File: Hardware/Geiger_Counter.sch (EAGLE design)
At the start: 54 parts, among them Q1 MPSA42, Q2 MPSA18, Q3 MMBT4403, Q4 MPSA18, U10 FT232RL-BASICSSOP, U17 AVR_SPI_PRG_6PTH, U7 TRANSFORMERAUDIO, U8 ATMEGA168, X1 USBSMD

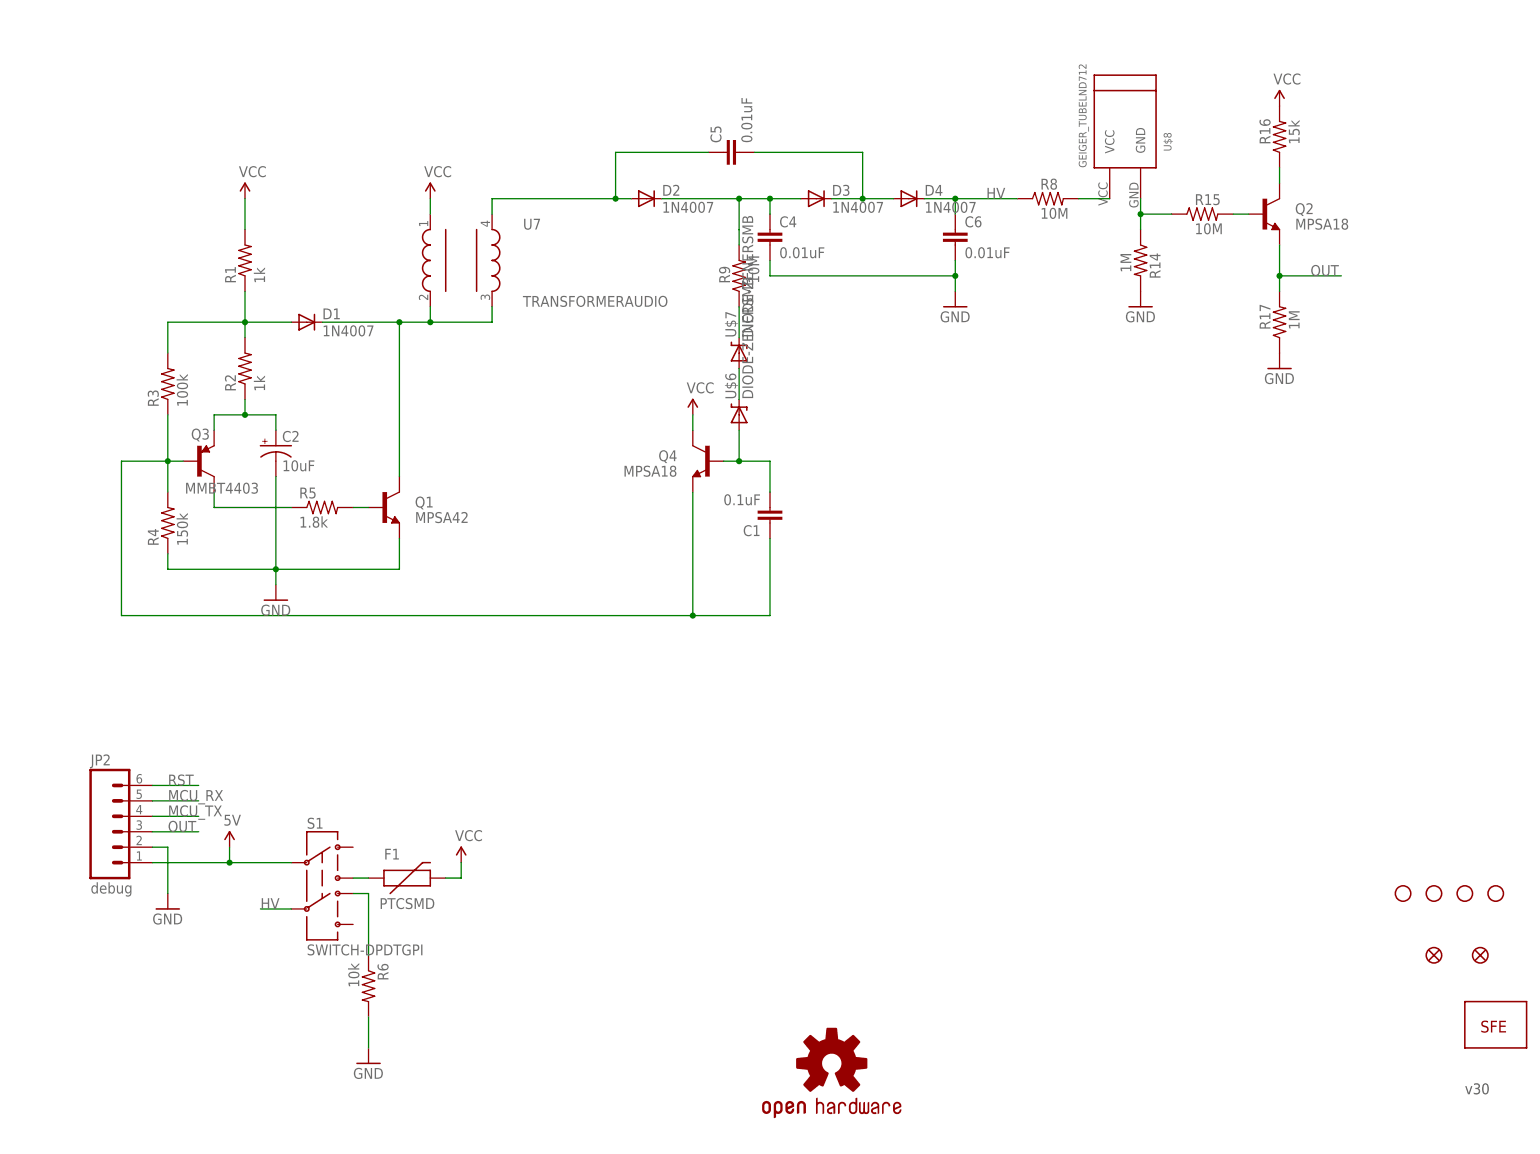
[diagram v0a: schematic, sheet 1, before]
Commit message: Updated cap/res trace re work
Updated all caps and res to 0603
Re routed y junctions to "t" junctions
Added "high voltage" to btm silk
updated schematic to frame letter.
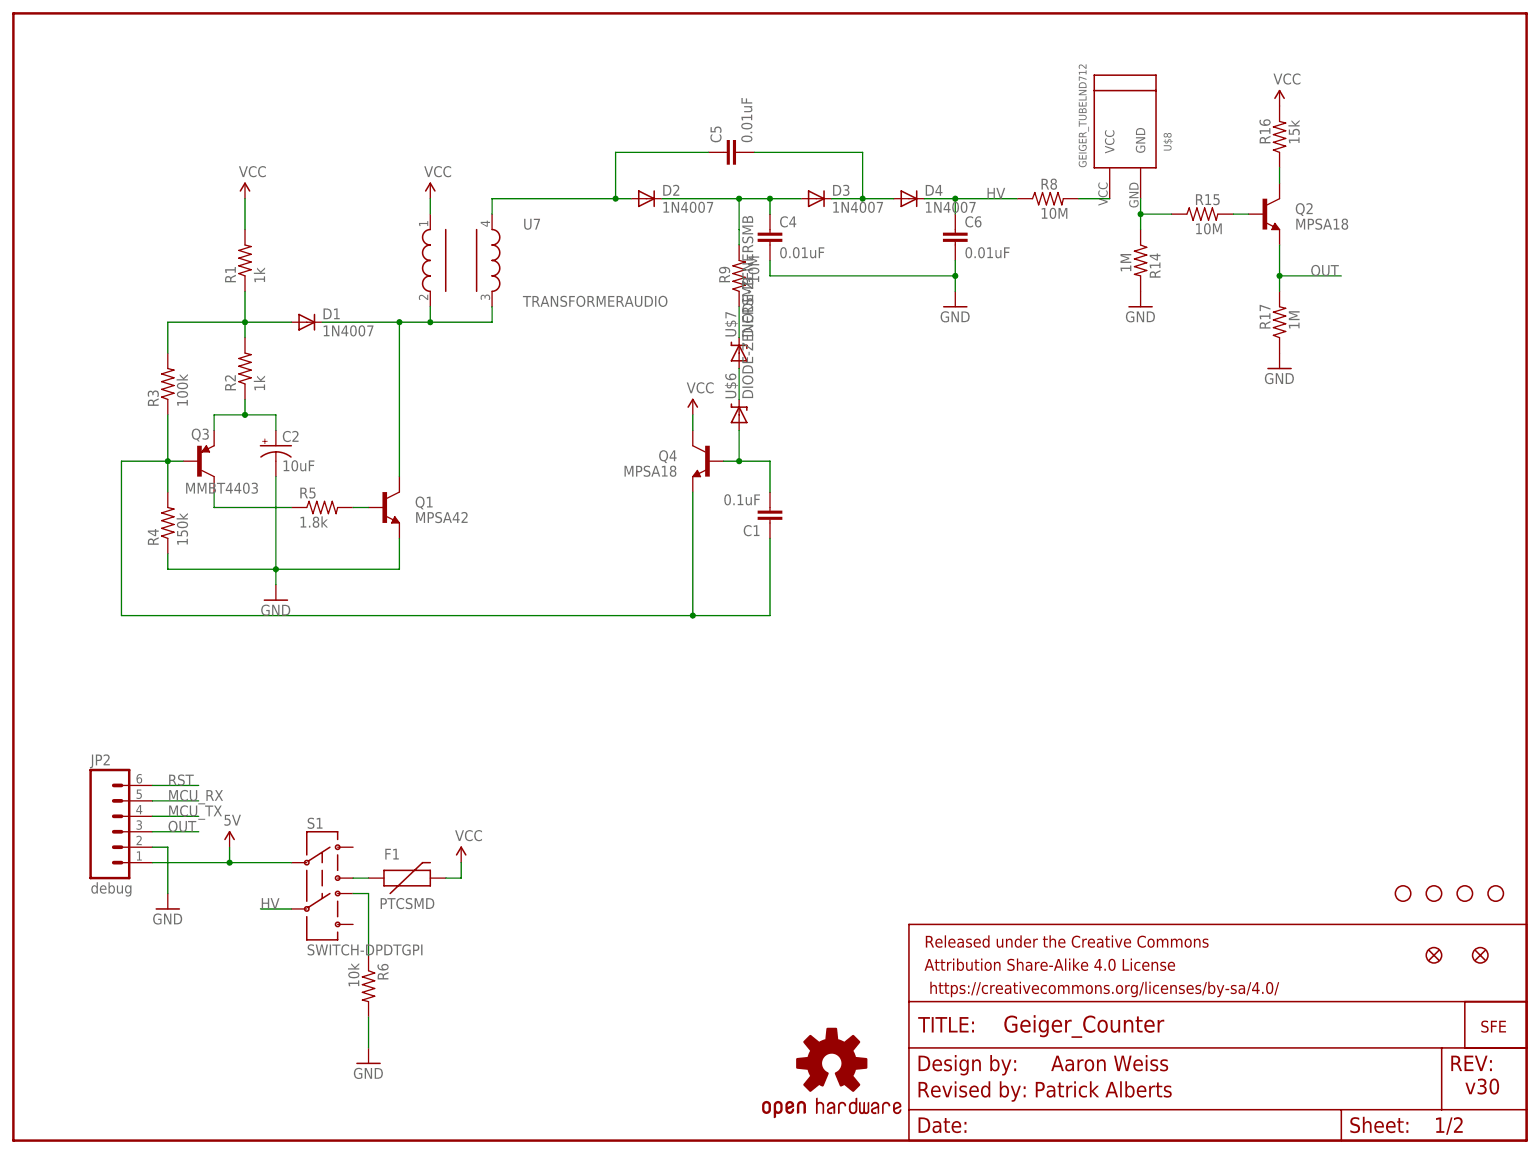
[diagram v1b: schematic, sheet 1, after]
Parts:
- added FRAME1: FRAME-LETTER, SparkFun-Aesthetics:FRAME-LETTER
- C1: device SparkFun-Capacitors:CAP0402-CAP -> SparkFun-Capacitors:0.1UF-25V(+80/-20%)(0603)
- C11, C3, C7: device SparkFun:CAP0402-CAP -> SparkFun-Capacitors:0.1UF-25V(+80/-20%)(0603)
- R1, R2: device SparkFun:RESISTOR0402-RES -> SparkFun-Resistors:1KOHM1/10W1%(0603)
- R11: device SparkFun:RESISTOR0402-RES -> SparkFun-Resistors:10KOHM1/10W1%(0603)0603
- R12: device SparkFun:RESISTOR0402-RES -> SparkFun-Resistors:33OHM1/10W1%(0603)
- R13: device SparkFun:RESISTOR0402-RES -> SparkFun-Resistors:330OHM1/10W1%(0603)
- R3: device SparkFun:RESISTOR0402-RES -> SparkFun-Resistors:100KOHM1/10W1%(0603)
- R4: device SparkFun:RESISTOR0402-RES -> SparkFun-Resistors:150KOHM1/10W1%(0603)
- R5: device SparkFun:RESISTOR0402-RES -> SparkFun-Resistors:1.8KOHM1/10W1%(0603)
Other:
- note added: "Aaron Weiss"
- note added: "Revised by: Patrick Alberts"
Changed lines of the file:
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@@
 <layer number="106" name="bPlate" color="7" fill="1" visible="yes" active="yes"/>
 <layer number="107" name="Crop" color="7" fill="1" visible="yes" active="yes"/>
+<layer number="108" name="tplace-old" color="10" fill="1" visible="no" active="yes"/>
+<layer number="109" name="ref-old" color="11" fill="1" visible="no" active="yes"/>
 <layer number="116" name="Patch_BOT" color="9" fill="4" visible="yes" active="yes"/>
 <layer number="121" name="_tsilk" color="7" fill="1" visible="yes" active="yes"/>
@@
 <layer number="144" name="Drill_legend" color="7" fill="1" visible="yes" active="yes"/>
 <layer number="151" name="HeatSink" color="7" fill="1" visible="yes" active="yes"/>
+<layer number="199" name="Contour" color="7" fill="1" visible="yes" active="yes"/>
 <layer number="200" name="200bmp" color="1" fill="10" visible="no" active="no"/>
 <layer number="201" name="201bmp" color="2" fill="1" visible="no" active="no"/>
@@
 </classes>
 <parts>
-<part name="FRAME1" library="SparkFun" deviceset="FRAME-LETTER" device=""/>
-<part name="R1" library="SparkFun" deviceset="RESISTOR" device="0402-RES" value="1k"/>
-<part name="R2" library="SparkFun" deviceset="RESISTOR" device="0402-RES" value="1k"/>
-<part name="R3" library="SparkFun" deviceset="RESISTOR" device="0402-RES" value="100k"/>
-<part name="R4" library="SparkFun" deviceset="RESISTOR" device="0402-RES" value="150k"/>
-<part name="R5" library="SparkFun" deviceset="RESISTOR" device="0402-RES" value="1.8k"/>
+<part name="FRAME1" library="SparkFun-Aesthetics" deviceset="FRAME-LETTER" device=""/>
+<part name="R1" library="SparkFun-Resistors" deviceset="1KOHM1/10W1%(0603)" device="" value="1k"/>
+<part name="R2" library="SparkFun-Resistors" deviceset="1KOHM1/10W1%(0603)" device="" value="1k"/>
+<part name="R3" library="SparkFun-Resistors" deviceset="100KOHM1/10W1%(0603)" device="" value="100k"/>
+<part name="R4" library="SparkFun-Resistors" deviceset="150KOHM1/10W1%(0603)" device="" value="150k"/>
+<part name="R5" library="SparkFun-Resistors" deviceset="1.8KOHM1/10W1%(0603)" device="" value="1.8k"/>
 <part name="D1" library="SparkFun" deviceset="DIODE" device="HV" value="1N4007"/>
 <part name="D2" library="SparkFun" deviceset="DIODE" device="PTH" value="1N4007"/>
@@
 <part name="U8" library="SparkFun" deviceset="ATMEGA168" device=""/>
 <part name="U$16" library="SparkFun" deviceset="5V" device=""/>
-<part name="R11" library="SparkFun" deviceset="RESISTOR" device="0402-RES" value="10k"/>
+<part name="R11" library="SparkFun-Resistors" deviceset="10KOHM1/10W1%(0603)" device="0603" value="10k"/>
 <part name="S2" library="SparkFun" deviceset="TAC_SWITCH" device="SMD" value="Reset"/>
 <part name="LED2" library="SparkFun" deviceset="LED" device="1206" value="Green"/>
@@
 <part name="GND13" library="SparkFun" deviceset="GND" device=""/>
 <part name="U$21" library="SparkFun" deviceset="5V" device=""/>
-<part name="C11" library="SparkFun" deviceset="CAP" device="0402-CAP" value="0.1uF"/>
-<part name="R13" library="SparkFun" deviceset="RESISTOR" device="0402-RES" value="330"/>
+<part name="C11" library="SparkFun-Capacitors" deviceset="0.1UF-25V(+80/-20%)(0603)" device="" value="0.1uF"/>
+<part name="R13" library="SparkFun-Resistors" deviceset="330OHM1/10W1%(0603)" device="" value="330"/>
 <part name="U$22" library="SparkFun" deviceset="5V" device=""/>
 <part name="U10" library="SparkFun" deviceset="FT232RL-BASIC" device="SSOP"/>
 <part name="X1" library="SparkFun" deviceset="USB" device="SMD"/>
-<part name="C7" library="SparkFun" deviceset="CAP" device="0402-CAP" value="0.1uF"/>
+<part name="C7" library="SparkFun-Capacitors" deviceset="0.1UF-25V(+80/-20%)(0603)" device="" value="0.1uF"/>
 <part name="C10" library="SparkFun" deviceset="CAP_POL" device="1206" value="10uF"/>
 <part name="U$19" library="SparkFun" deviceset="5V" device=""/>
 <part name="GND1" library="SparkFun" deviceset="GND" device=""/>
 <part name="GND3" library="SparkFun" deviceset="GND" device=""/>
-<part name="R12" library="SparkFun" deviceset="RESISTOR" device="0402-RES" value="330"/>
+<part name="R12" library="SparkFun-Resistors" deviceset="33OHM1/10W1%(0603)" device="" value="330"/>
 <part name="LED1" library="SparkFun" deviceset="LED" device="1206" value="Red"/>
 <part name="GND9" library="SparkFun" deviceset="GND" device=""/>
 <part name="GND4" library="SparkFun" deviceset="GND" device=""/>
-<part name="C3" library="SparkFun" deviceset="CAP" device="0402-CAP" value="0.1uF"/>
+<part name="C3" library="SparkFun-Capacitors" deviceset="0.1UF-25V(+80/-20%)(0603)" device="" value="0.1uF"/>
 <part name="R14" library="SparkFun" deviceset="RESISTOR" device="AXIAL-0.3" value="1M"/>
 <part name="R15" library="SparkFun" deviceset="RESISTOR" device="AXIAL-0.3" value="10M"/>
@@
 <part name="U$7" library="SparkFun-DiscreteSemi" deviceset="DIODE-ZENER" device="SMB"/>
 <part name="R9" library="SparkFun" deviceset="RESISTOR" device="AXIAL-0.3" value="10M"/>
-<part name="C1" library="SparkFun-Capacitors" deviceset="CAP" device="0402-CAP" value="0.1uF"/>
+<part name="C1" library="SparkFun-Capacitors" deviceset="0.1UF-25V(+80/-20%)(0603)" device="" value="0.1uF"/>
 <part name="JP1" library="SparkFun" deviceset="FIDUCIAL" device="UFIDUCIAL"/>
 <part name="JP3" library="SparkFun" deviceset="FIDUCIAL" device="UFIDUCIAL"/>
@@
 <sheet>
 <plain>
-<text x="238.76" y="7.62" size="1.778" layer="97">v30</text>
+<text x="238.76" y="7.62" size="2.54" layer="94">v30</text>
+<text x="170.688" y="11.43" size="2.54" layer="94">Aaron Weiss</text>
+<text x="148.59" y="7.112" size="2.54" layer="94">Revised by: Patrick Alberts</text>
 </plain>
 <instances>

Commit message: Schematic Cleanup / Trace redo
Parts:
- FRAME1: value FRAME-LETTER -> FRAME-LEDGER; device SparkFun-Aesthetics:FRAME-LETTER -> SparkFun-Aesthetics:FRAME-LEDGER
